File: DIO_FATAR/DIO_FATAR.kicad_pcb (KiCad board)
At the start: 2 copper layers, 100 x 55 mm, 20 parts, among them J1 in, J2 thru, J3 right, J4 left, U1 74HC595, U2 74HC595, U3 74165, U4 74165

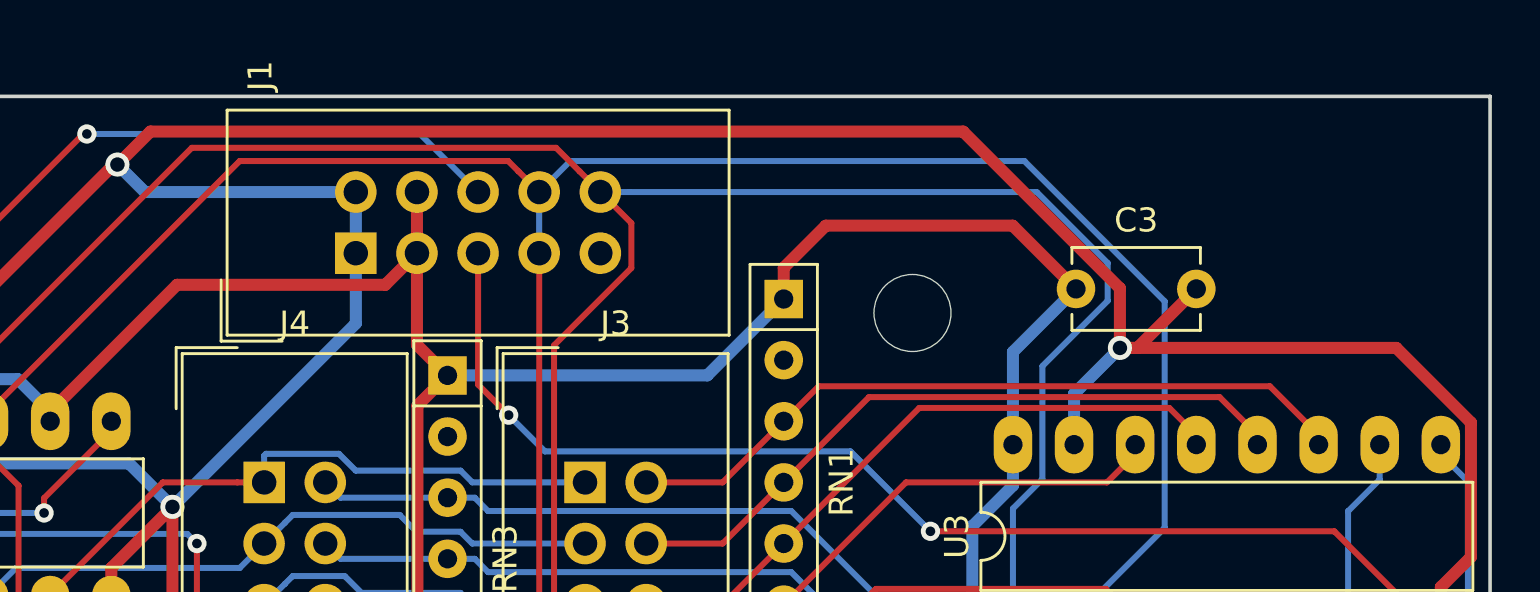
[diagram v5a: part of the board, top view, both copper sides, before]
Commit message: DIO_FATAR: route remaining resistors
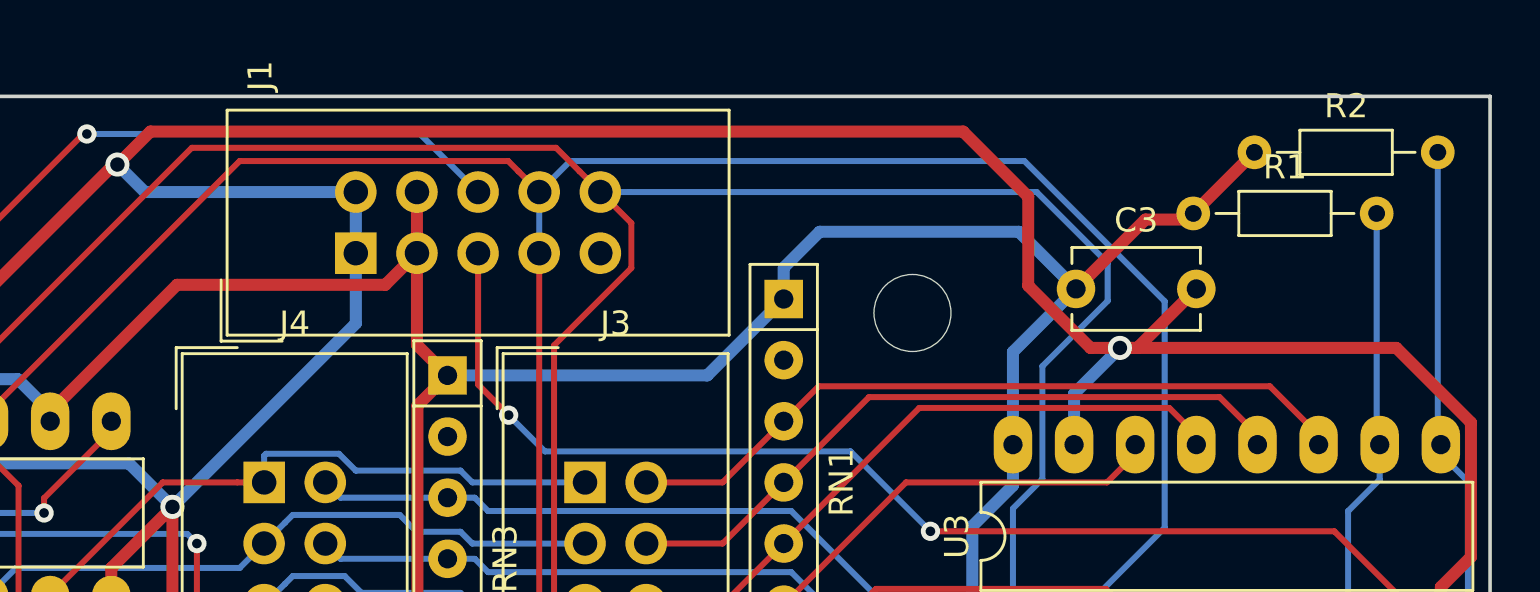
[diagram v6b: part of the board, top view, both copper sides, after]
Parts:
- added R1: 10k, Resistor_THT:R_Axial_DIN0204_L3.6mm_D1.6mm_P7.62mm_Horizontal, F.Cu at (137.7, 54.9)
- added R2: 10k, Resistor_THT:R_Axial_DIN0204_L3.6mm_D1.6mm_P7.62mm_Horizontal, F.Cu at (140.2, 52.3)
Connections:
- RN2 pad 2: /SI_THRU -> Net-(RN2-Pad2)
- U3 pad 9: Net-(RN3-Pad2) -> Net-(R2-Pad2)
- U4 pad 10: Net-(RN3-Pad2) -> Net-(R2-Pad2)
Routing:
- net Net-(R2-Pad2): track 0.00 -> 28.2 mm
- net Net-(RN3-Pad2): track 16.0 -> 0.00 mm
- net +5V: track 205.7 -> 215.4 mm
- net /SI_THRU: track 66.2 -> 75.6 mm
- net GND: track 320.2 -> 320.9 mm

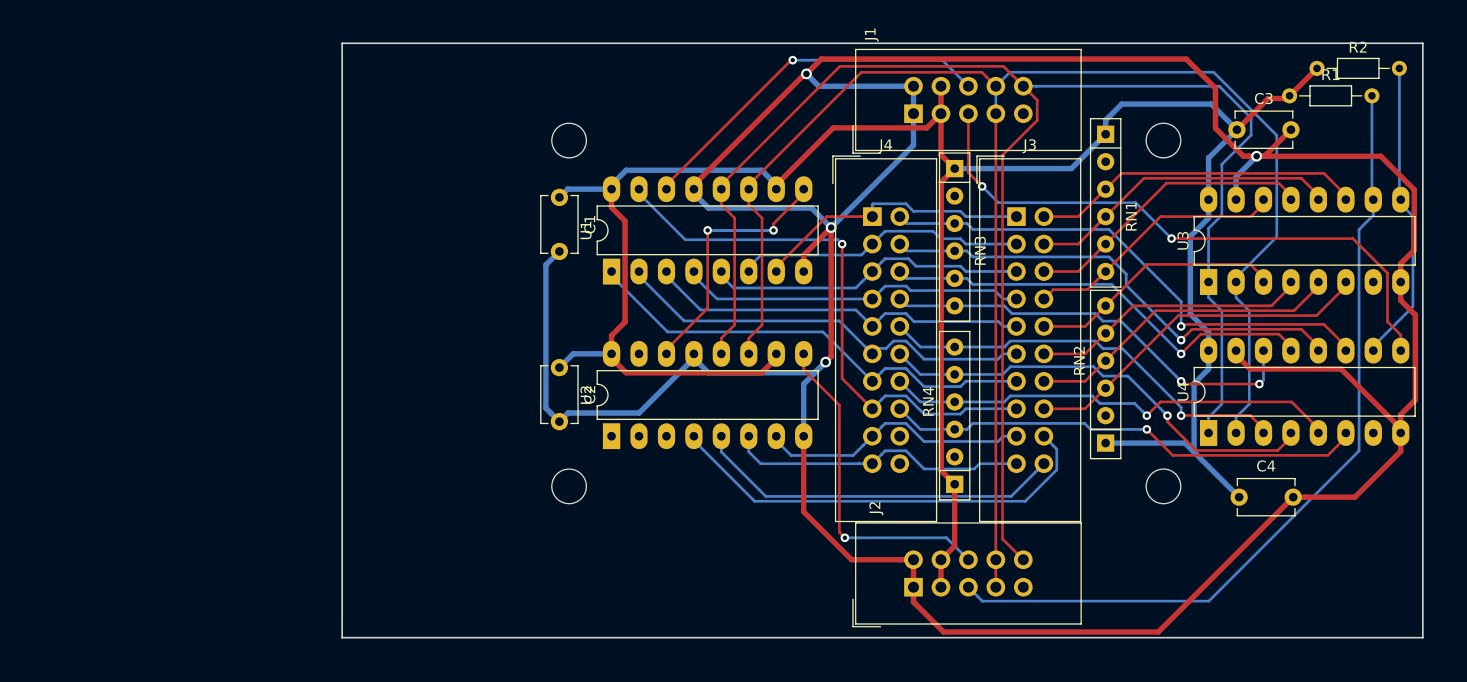
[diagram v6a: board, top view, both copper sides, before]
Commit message: DIO_FATAR: adjust edge cuts
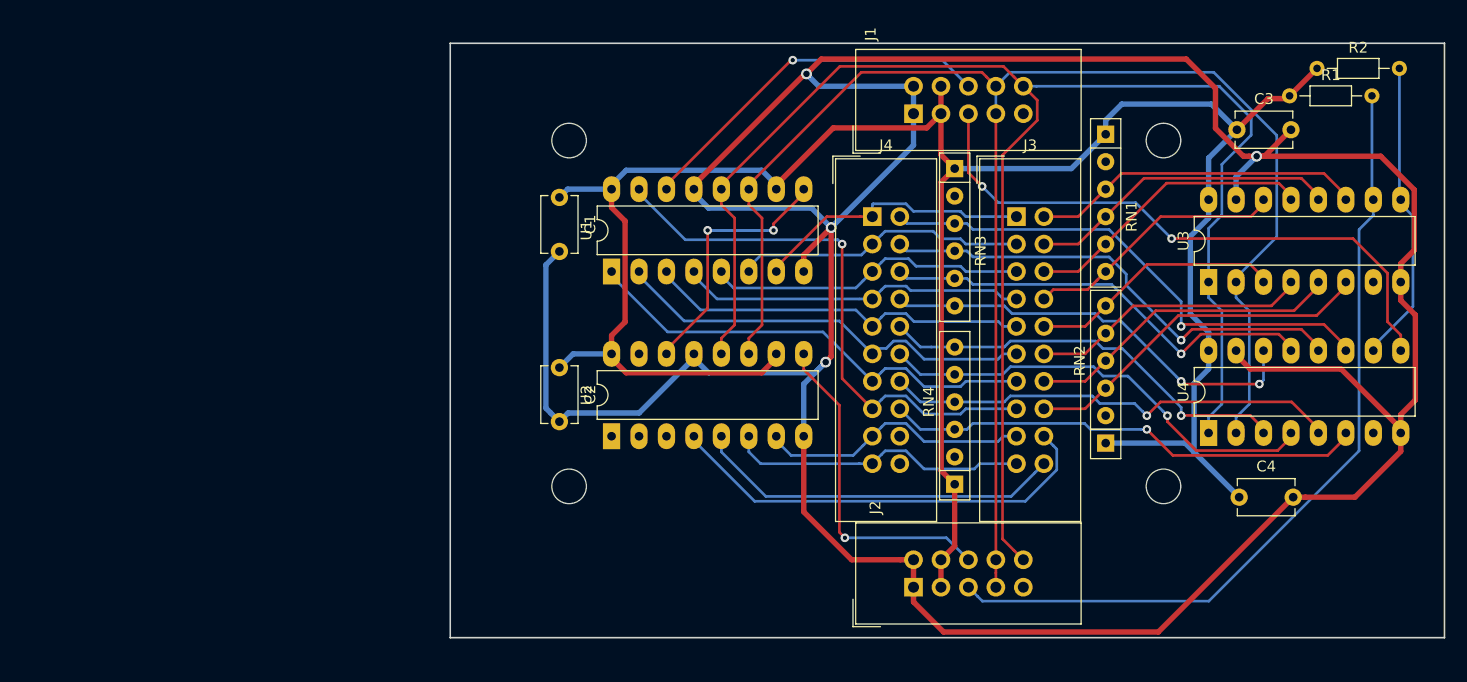
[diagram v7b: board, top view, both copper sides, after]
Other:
- board size 100 x 55 mm -> 92 x 55 mm
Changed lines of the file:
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@@
     (pad 1 np_thru_hole circle (at 0 0) (size 3.2 3.2) (drill 3.2) (layers *.Cu *.Mask))
   )
-  (gr_line (start 50 105) (end 50 50) (layer Edge.Cuts) (width 0.15))
-  (gr_line (start 150 105) (end 50 105) (layer Edge.Cuts) (width 0.15))
-  (gr_line (start 150 50) (end 150 105) (layer Edge.Cuts) (width 0.15))
-  (gr_line (start 50 50) (end 150 50) (layer Edge.Cuts) (width 0.15))
+  (gr_line (start 60 105) (end 60 50) (layer Edge.Cuts) (width 0.15))
+  (gr_line (start 152 105) (end 60 105) (layer Edge.Cuts) (width 0.15))
+  (gr_line (start 152 50) (end 152 105) (layer Edge.Cuts) (width 0.15))
+  (gr_line (start 60 50) (end 152 50) (layer Edge.Cuts) (width 0.15))
   (segment (start 130.175 76.74) (end 130.175 78.44) (width 0.5) (layer B.Cu) (net 1))
   (segment (start 128.485001 75.050001) (end 130.175 76.74) (width 0.5) (layer B.Cu) (net 1))

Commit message: DIO_FATAR: finalize
 - add fills
 - adjust cuts once more
 - move R1, R2
 - move part references
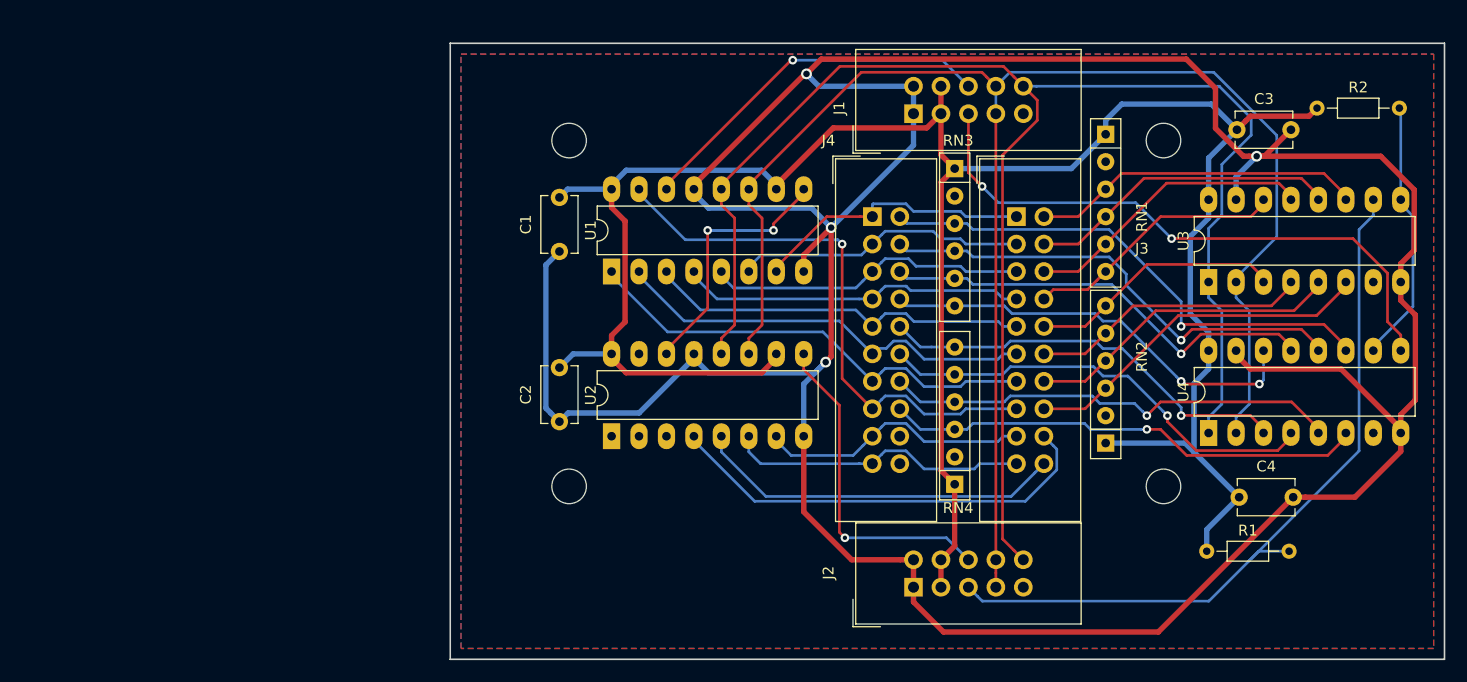
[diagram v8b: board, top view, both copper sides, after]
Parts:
- ? (x4): value MountingHole_3.2mm_M3_DIN965 -> (none)
- moved R1 42.8 mm to (130.0, 97.0)
- moved R2 3.68 mm to (140.2, 56.0)
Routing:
- net /SI_THRU: track 75.6 -> 70.3 mm
- net +5V: track 215.4 -> 220.0 mm
- net Net-(R2-Pad2): track 28.2 -> 24.7 mm
- added copper zone on B.Cu, net GND
- added copper zone on F.Cu, net GND
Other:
- board size 92 x 55 mm -> 92 x 57 mm
